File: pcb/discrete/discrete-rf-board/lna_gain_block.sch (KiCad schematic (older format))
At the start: 21 parts, among them Q801 Q_NPN_BCEE

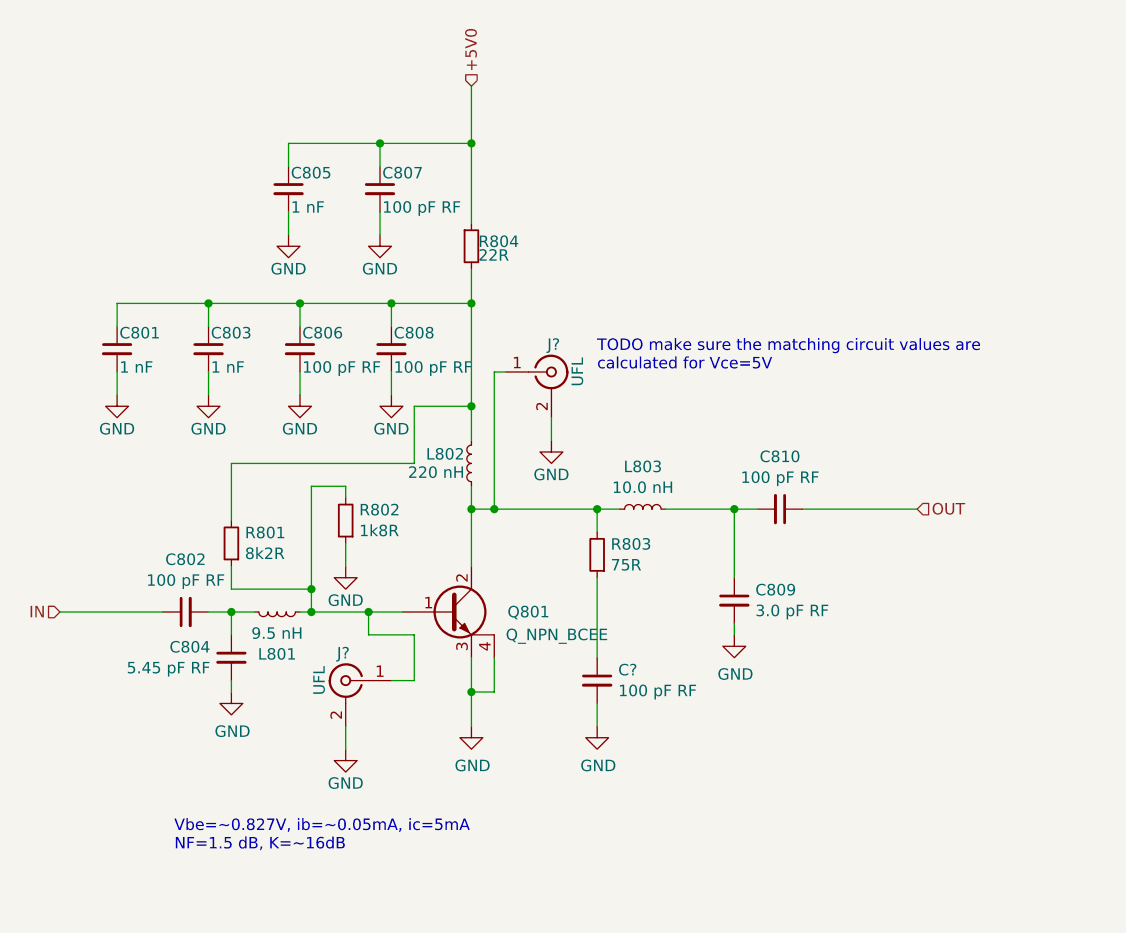
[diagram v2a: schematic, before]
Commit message: Start work in footprinting everything
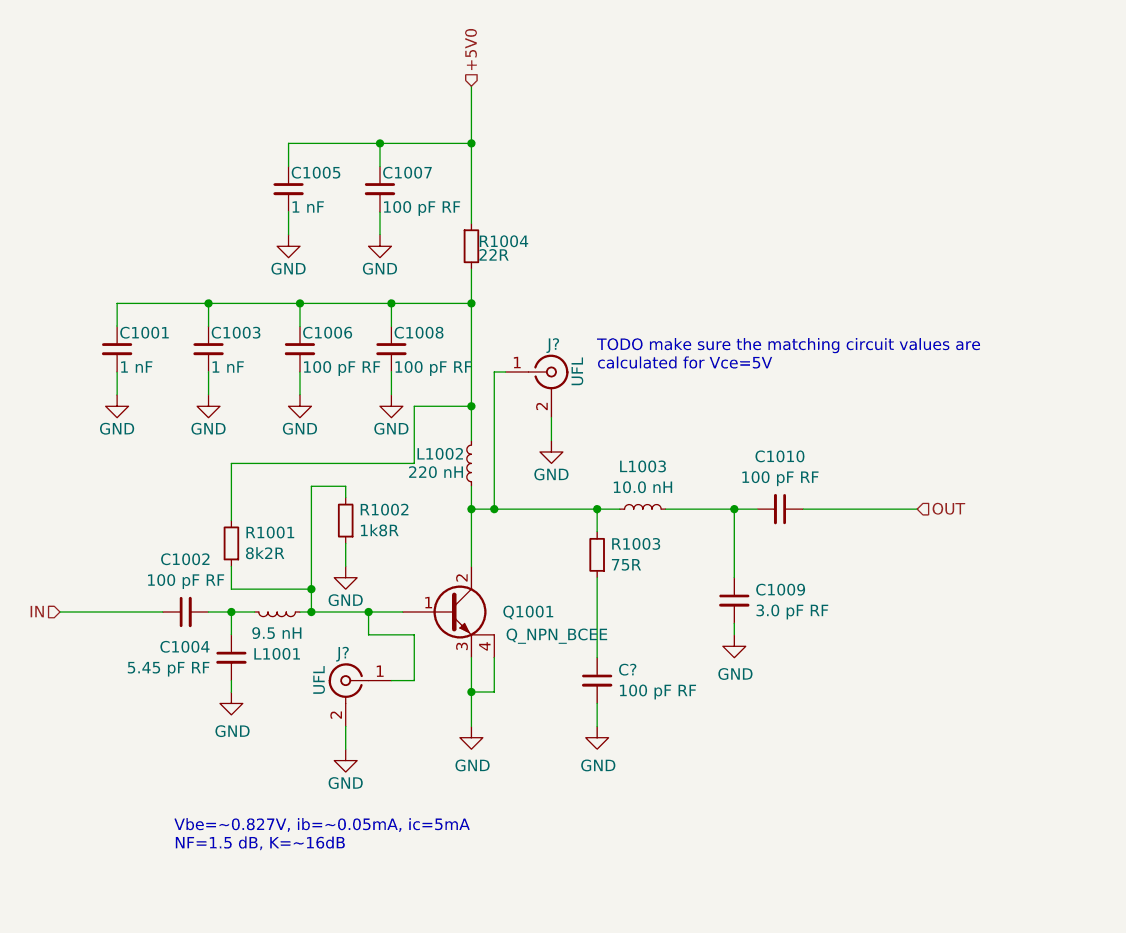
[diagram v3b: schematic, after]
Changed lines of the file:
@@
 AR Path="/5CA6B0AA/5CE74EBE/5D4104E7/5D3CF638" Ref="R903"  Part="1"
 AR Path="/5CA6B0AA/5CE74EBE/5D4124AC/5D3CF638" Ref="R1003"  Part="1"
-F 0 "R803" H 6041 3404 50  0000 R CNN
+F 0 "R1003" H 6041 3404 50  0000 R CNN
 F 1 "75R" H 6041 3495 50  0000 R CNN
 F 2 "" H 6100 3450 50  0001 C CNN
@@
 AR Path="/5CA6B0AA/5CE74EBE/5D4104E7/5D3CF640" Ref="C910"  Part="1"
 AR Path="/5CA6B0AA/5CE74EBE/5D4124AC/5D3CF640" Ref="C1010"  Part="1"
-F 0 "C810" V 7129 3250 50  0000 C CNN
+F 0 "C1010" V 7129 3250 50  0000 C CNN
 F 1 "100 pF RF" V 7038 3250 50  0000 C CNN
 F 2 "" H 6900 3250 50  0001 C CNN
@@
 AR Path="/5CA6B0AA/5CE74EBE/5D4104E7/5D3CF649" Ref="#PWR0903"  Part="1"
 AR Path="/5CA6B0AA/5CE74EBE/5D4124AC/5D3CF649" Ref="#PWR01003"  Part="1"
-F 0 "#PWR0803" H 4500 3800 50  0001 C CNN
+F 0 "#PWR01003" H 4500 3800 50  0001 C CNN
 F 1 "GND" H 4505 3877 50  0000 C CNN
 F 2 "" H 4500 4050 50  0001 C CNN
@@
 AR Path="/5CA6B0AA/5CE74EBE/5D4104E7/5D3CF650" Ref="#PWR0910"  Part="1"
 AR Path="/5CA6B0AA/5CE74EBE/5D4124AC/5D3CF650" Ref="#PWR01010"  Part="1"
-F 0 "#PWR0810" H 6700 3550 50  0001 C CNN
+F 0 "#PWR01010" H 6700 3550 50  0001 C CNN
 F 1 "GND" H 6705 3627 50  0000 C CNN
 F 2 "" H 6700 3800 50  0001 C CNN
@@
 AR Path="/5CA6B0AA/5CE74EBE/5D4104E7/5D3CF659" Ref="R901"  Part="1"
 AR Path="/5CA6B0AA/5CE74EBE/5D4124AC/5D3CF659" Ref="R1001"  Part="1"
-F 0 "R801" H 4441 3354 50  0000 R CNN
+F 0 "R1001" H 4441 3354 50  0000 R CNN
 F 1 "8k2R" H 4441 3445 50  0000 R CNN
 F 2 "" H 4500 3400 50  0001 C CNN
@@
 AR Path="/5CA6B0AA/5CE74EBE/5D4104E7/5D3CF668" Ref="C909"  Part="1"
 AR Path="/5CA6B0AA/5CE74EBE/5D4124AC/5D3CF668" Ref="C1009"  Part="1"
-F 0 "C809" H 6792 3696 50  0000 L CNN
+F 0 "C1009" H 6792 3696 50  0000 L CNN
 F 1 "3.0 pF RF" H 6792 3605 50  0000 L CNN
 F 2 "" H 6700 3650 50  0001 C CNN
@@
 AR Path="/5CA6B0AA/5CE74EBE/5D4104E7/5D3CF670" Ref="L903"  Part="1"
 AR Path="/5CA6B0AA/5CE74EBE/5D4124AC/5D3CF670" Ref="L1003"  Part="1"
-F 0 "L803" V 6485 3250 50  0000 C CNN
+F 0 "L1003" V 6485 3250 50  0000 C CNN
 F 1 "10.0 nH" V 6394 3250 50  0000 C CNN
 F 2 "" H 6300 3250 50  0001 C CNN
@@
 AR Path="/5CA6B0AA/5CE74EBE/5D4104E7/5D3CF693" Ref="C902"  Part="1"
 AR Path="/5CA6B0AA/5CE74EBE/5D4124AC/5D3CF693" Ref="C1002"  Part="1"
-F 0 "C802" V 4529 3700 50  0000 C CNN
+F 0 "C1002" V 4529 3700 50  0000 C CNN
 F 1 "100 pF RF" V 4438 3700 50  0000 C CNN
 F 2 "" H 4300 3700 50  0001 C CNN
@@
 AR Path="/5CA6B0AA/5CE74EBE/5D4104E7/5D3CF699" Ref="L901"  Part="1"
 AR Path="/5CA6B0AA/5CE74EBE/5D4124AC/5D3CF699" Ref="L1001"  Part="1"
-F 0 "L801" V 4885 3700 50  0000 C CNN
+F 0 "L1001" V 4885 3700 50  0000 C CNN
 F 1 "9.5 nH" V 4794 3700 50  0000 C CNN
 F 2 "" H 4700 3700 50  0001 C CNN
@@
 AR Path="/5CA6B0AA/5CE74EBE/5D4104E7/5D3CF69F" Ref="C904"  Part="1"
 AR Path="/5CA6B0AA/5CE74EBE/5D4124AC/5D3CF69F" Ref="C1004"  Part="1"
-F 0 "C804" H 4592 3946 50  0000 L CNN
+F 0 "C1004" H 4592 3946 50  0000 L CNN
 F 1 "5.45 pF RF" H 4592 3855 50  0000 L CNN
 F 2 "" H 4500 3900 50  0001 C CNN
@@
 AR Path="/5CA6B0AA/5CE74EBE/5D4104E7/5D3CF6A6" Ref="#PWR0909"  Part="1"
 AR Path="/5CA6B0AA/5CE74EBE/5D4124AC/5D3CF6A6" Ref="#PWR01009"  Part="1"
-F 0 "#PWR0809" H 5550 3950 50  0001 C CNN
+F 0 "#PWR01009" H 5550 3950 50  0001 C CNN
 F 1 "GND" H 5555 4027 50  0000 C CNN
 F 2 "" H 5550 4200 50  0001 C CNN
@@
 AR Path="/5CA6B0AA/5CE74EBE/5D4104E7/5D3E5B01" Ref="C903"  Part="1"
 AR Path="/5CA6B0AA/5CE74EBE/5D4124AC/5D3E5B01" Ref="C1003"  Part="1"
-F 0 "C803" H 4410 2620 50  0000 L CNN
+F 0 "C1003" H 4410 2620 50  0000 L CNN
 F 1 "1 nF" H 4410 2470 50  0000 L CNN
 F 2 "" H 4400 2550 50  0001 C CNN
@@
 AR Path="/5CA6B0AA/5CE74EBE/5D4104E7/5D3E5B07" Ref="C906"  Part="1"
 AR Path="/5CA6B0AA/5CE74EBE/5D4124AC/5D3E5B07" Ref="C1006"  Part="1"
-F 0 "C806" H 4810 2620 50  0000 L CNN
+F 0 "C1006" H 4810 2620 50  0000 L CNN
 F 1 "100 pF RF" H 4810 2470 50  0000 L CNN
 F 2 "" H 4800 2550 50  0001 C CNN
@@
 AR Path="/5CA6B0AA/5CE74EBE/5D4104E7/5D3E5B0D" Ref="C908"  Part="1"
 AR Path="/5CA6B0AA/5CE74EBE/5D4124AC/5D3E5B0D" Ref="C1008"  Part="1"
-F 0 "C808" H 5210 2620 50  0000 L CNN
+F 0 "C1008" H 5210 2620 50  0000 L CNN
 F 1 "100 pF RF" H 5210 2470 50  0000 L CNN
 F 2 "" H 5200 2550 50  0001 C CNN
@@
 AR Path="/5CA6B0AA/5CE74EBE/5D4104E7/5D3E5B13" Ref="#PWR0902"  Part="1"
 AR Path="/5CA6B0AA/5CE74EBE/5D4124AC/5D3E5B13" Ref="#PWR01002"  Part="1"
-F 0 "#PWR0802" H 4400 2500 50  0001 C CNN
+F 0 "#PWR01002" H 4400 2500 50  0001 C CNN
 F 1 "GND" H 4400 2600 50  0000 C CNN
 F 2 "" H 4400 2750 50  0001 C CNN
@@
 AR Path="/5CA6B0AA/5CE74EBE/5D4104E7/5D3E5B19" Ref="#PWR0905"  Part="1"
 AR Path="/5CA6B0AA/5CE74EBE/5D4124AC/5D3E5B19" Ref="#PWR01005"  Part="1"
-F 0 "#PWR0805" H 4800 2500 50  0001 C CNN
+F 0 "#PWR01005" H 4800 2500 50  0001 C CNN
 F 1 "GND" H 4800 2600 50  0000 C CNN
 F 2 "" H 4800 2750 50  0001 C CNN
@@
 AR Path="/5CA6B0AA/5CE74EBE/5D4104E7/5D3E5B1F" Ref="#PWR0908"  Part="1"
 AR Path="/5CA6B0AA/5CE74EBE/5D4124AC/5D3E5B1F" Ref="#PWR01008"  Part="1"
-F 0 "#PWR0808" H 5200 2500 50  0001 C CNN
+F 0 "#PWR01008" H 5200 2500 50  0001 C CNN
 F 1 "GND" H 5200 2600 50  0000 C CNN
 F 2 "" H 5200 2750 50  0001 C CNN
@@
 AR Path="/5CA6B0AA/5CE74EBE/5D4104E7/5D3E5B25" Ref="C907"  Part="1"
 AR Path="/5CA6B0AA/5CE74EBE/5D4124AC/5D3E5B25" Ref="C1007"  Part="1"
-F 0 "C807" H 5160 1920 50  0000 L CNN
+F 0 "C1007" H 5160 1920 50  0000 L CNN
 F 1 "100 pF RF" H 5160 1770 50  0000 L CNN
 F 2 "" H 5150 1850 50  0001 C CNN
@@
 AR Path="/5CA6B0AA/5CE74EBE/5D4104E7/5D3E5B2B" Ref="#PWR0907"  Part="1"
 AR Path="/5CA6B0AA/5CE74EBE/5D4124AC/5D3E5B2B" Ref="#PWR01007"  Part="1"
-F 0 "#PWR0807" H 5150 1800 50  0001 C CNN
+F 0 "#PWR01007" H 5150 1800 50  0001 C CNN
 F 1 "GND" H 5150 1900 50  0000 C CNN
 F 2 "" H 5150 2050 50  0001 C CNN
@@
 AR Path="/5CA6B0AA/5CE74EBE/5D4104E7/5D3E5B31" Ref="C905"  Part="1"
 AR Path="/5CA6B0AA/5CE74EBE/5D4124AC/5D3E5B31" Ref="C1005"  Part="1"
-F 0 "C805" H 4760 1920 50  0000 L CNN
+F 0 "C1005" H 4760 1920 50  0000 L CNN
 F 1 "1 nF" H 4760 1770 50  0000 L CNN
 F 2 "" H 4750 1850 50  0001 C CNN
@@
 AR Path="/5CA6B0AA/5CE74EBE/5D4104E7/5D3E5B37" Ref="#PWR0904"  Part="1"
 AR Path="/5CA6B0AA/5CE74EBE/5D4124AC/5D3E5B37" Ref="#PWR01004"  Part="1"
-F 0 "#PWR0804" H 4750 1800 50  0001 C CNN
+F 0 "#PWR01004" H 4750 1800 50  0001 C CNN
 F 1 "GND" H 4750 1900 50  0000 C CNN
 F 2 "" H 4750 2050 50  0001 C CNN
@@
 AR Path="/5CA6B0AA/5CE74EBE/5D4104E7/5D3F1C48" Ref="R904"  Part="1"
 AR Path="/5CA6B0AA/5CE74EBE/5D4124AC/5D3F1C48" Ref="R1004"  Part="1"
-F 0 "R804" H 5580 2120 50  0000 L CNN
+F 0 "R1004" H 5580 2120 50  0000 L CNN
 F 1 "22R" H 5580 2060 50  0000 L CNN
 F 2 "" H 5550 2100 50  0001 C CNN
@@
 AR Path="/5CA6B0AA/5CE74EBE/5D4104E7/5D3FEB6E" Ref="C901"  Part="1"
 AR Path="/5CA6B0AA/5CE74EBE/5D4124AC/5D3FEB6E" Ref="C1001"  Part="1"
-F 0 "C801" H 4010 2620 50  0000 L CNN
+F 0 "C1001" H 4010 2620 50  0000 L CNN
 F 1 "1 nF" H 4010 2470 50  0000 L CNN
 F 2 "" H 4000 2550 50  0001 C CNN
@@
 AR Path="/5CA6B0AA/5CE74EBE/5D4104E7/5D3FEB74" Ref="#PWR0901"  Part="1"
 AR Path="/5CA6B0AA/5CE74EBE/5D4124AC/5D3FEB74" Ref="#PWR01001"  Part="1"
-F 0 "#PWR0801" H 4000 2500 50  0001 C CNN
+F 0 "#PWR01001" H 4000 2500 50  0001 C CNN
 F 1 "GND" H 4000 2600 50  0000 C CNN
 F 2 "" H 4000 2750 50  0001 C CNN
@@
 AR Path="/5CA6B0AA/5CE74EBE/5D4104E7/5D40D244" Ref="L902"  Part="1"
 AR Path="/5CA6B0AA/5CE74EBE/5D4124AC/5D40D244" Ref="L1002"  Part="1"
-F 0 "L802" H 5580 3090 50  0000 L CNN
+F 0 "L1002" H 5580 3090 50  0000 L CNN
 F 1 "220 nH" H 5580 3010 50  0000 L CNN
 F 2 "" H 5550 3050 50  0001 C CNN
@@
 AR Path="/5CA6B0AA/5CE74EBE/5D4104E7/5D435867" Ref="R902"  Part="1"
 AR Path="/5CA6B0AA/5CE74EBE/5D4124AC/5D435867" Ref="R1002"  Part="1"
-F 0 "R802" H 4941 3254 50  0000 R CNN
+F 0 "R1002" H 4941 3254 50  0000 R CNN
 F 1 "1k8R" H 4941 3345 50  0000 R CNN
 F 2 "" H 5000 3300 50  0001 C CNN
@@
 AR Path="/5CA6B0AA/5CE74EBE/5D3C8D48/5D43681D" Ref="#PWR0806"  Part="1"
 AR Path="/5CA6B0AA/5CE74EBE/5D4104E7/5D43681D" Ref="#PWR0906"  Part="1"
-F 0 "#PWR0806" H 5000 3250 50  0001 C CNN
+F 0 "#PWR01006" H 5000 3250 50  0001 C CNN
 F 1 "GND" H 5000 3350 50  0000 C CNN
 F 2 "" H 5000 3500 50  0001 C CNN
@@
 AR Path="/5CA6B0AA/5CE74EBE/5D4104E7/5D191C23" Ref="Q901"  Part="1"
 AR Path="/5CA6B0AA/5CE74EBE/5D4124AC/5D191C23" Ref="Q1001"  Part="1"
-F 0 "Q801" H 5800 3700 50  0000 C CNN
+F 0 "Q1001" H 5800 3700 50  0000 C CNN
 F 1 "Q_NPN_BCEE" H 5700 3600 50  0000 L CNN
 F 2 "" H 5500 3700 50  0001 C CNN

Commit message: Fix some parts
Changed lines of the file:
@@
 $Descr A4 11693 8268
 encoding utf-8
-Sheet 16 19
+Sheet 14 19
 Title ""
 Date ""
@@
 AR Path="/5CA6B0AA/5CE74EBE/5D4104E7/5D3CF638" Ref="R903"  Part="1"
 AR Path="/5CA6B0AA/5CE74EBE/5D4124AC/5D3CF638" Ref="R1003"  Part="1"
-F 0 "R1003" H 6041 3404 50  0000 R CNN
+F 0 "R803" H 6041 3404 50  0000 R CNN
 F 1 "75R" H 6041 3495 50  0000 R CNN
 F 2 "" H 6100 3450 50  0001 C CNN
@@
 AR Path="/5CA6B0AA/5CE74EBE/5D4104E7/5D3CF640" Ref="C910"  Part="1"
 AR Path="/5CA6B0AA/5CE74EBE/5D4124AC/5D3CF640" Ref="C1010"  Part="1"
-F 0 "C1010" V 7129 3250 50  0000 C CNN
+F 0 "C810" V 7129 3250 50  0000 C CNN
 F 1 "100 pF RF" V 7038 3250 50  0000 C CNN
 F 2 "" H 6900 3250 50  0001 C CNN
@@
 AR Path="/5CA6B0AA/5CE74EBE/5D4104E7/5D3CF649" Ref="#PWR0903"  Part="1"
 AR Path="/5CA6B0AA/5CE74EBE/5D4124AC/5D3CF649" Ref="#PWR01003"  Part="1"
-F 0 "#PWR01003" H 4500 3800 50  0001 C CNN
+F 0 "#PWR0803" H 4500 3800 50  0001 C CNN
 F 1 "GND" H 4505 3877 50  0000 C CNN
 F 2 "" H 4500 4050 50  0001 C CNN
@@
 AR Path="/5CA6B0AA/5CE74EBE/5D4104E7/5D3CF650" Ref="#PWR0910"  Part="1"
 AR Path="/5CA6B0AA/5CE74EBE/5D4124AC/5D3CF650" Ref="#PWR01010"  Part="1"
-F 0 "#PWR01010" H 6700 3550 50  0001 C CNN
+F 0 "#PWR0810" H 6700 3550 50  0001 C CNN
 F 1 "GND" H 6705 3627 50  0000 C CNN
 F 2 "" H 6700 3800 50  0001 C CNN
@@
 AR Path="/5CA6B0AA/5CE74EBE/5D4104E7/5D3CF659" Ref="R901"  Part="1"
 AR Path="/5CA6B0AA/5CE74EBE/5D4124AC/5D3CF659" Ref="R1001"  Part="1"
-F 0 "R1001" H 4441 3354 50  0000 R CNN
+F 0 "R801" H 4441 3354 50  0000 R CNN
 F 1 "8k2R" H 4441 3445 50  0000 R CNN
 F 2 "" H 4500 3400 50  0001 C CNN
@@
 AR Path="/5CA6B0AA/5CE74EBE/5D4104E7/5D3CF668" Ref="C909"  Part="1"
 AR Path="/5CA6B0AA/5CE74EBE/5D4124AC/5D3CF668" Ref="C1009"  Part="1"
-F 0 "C1009" H 6792 3696 50  0000 L CNN
+F 0 "C809" H 6792 3696 50  0000 L CNN
 F 1 "3.0 pF RF" H 6792 3605 50  0000 L CNN
 F 2 "" H 6700 3650 50  0001 C CNN
@@
 AR Path="/5CA6B0AA/5CE74EBE/5D4104E7/5D3CF670" Ref="L903"  Part="1"
 AR Path="/5CA6B0AA/5CE74EBE/5D4124AC/5D3CF670" Ref="L1003"  Part="1"
-F 0 "L1003" V 6485 3250 50  0000 C CNN
+F 0 "L803" V 6485 3250 50  0000 C CNN
 F 1 "10.0 nH" V 6394 3250 50  0000 C CNN
 F 2 "" H 6300 3250 50  0001 C CNN
@@
 AR Path="/5CA6B0AA/5CE74EBE/5D4104E7/5D3CF693" Ref="C902"  Part="1"
 AR Path="/5CA6B0AA/5CE74EBE/5D4124AC/5D3CF693" Ref="C1002"  Part="1"
-F 0 "C1002" V 4529 3700 50  0000 C CNN
+F 0 "C802" V 4529 3700 50  0000 C CNN
 F 1 "100 pF RF" V 4438 3700 50  0000 C CNN
 F 2 "" H 4300 3700 50  0001 C CNN
@@
 AR Path="/5CA6B0AA/5CE74EBE/5D4104E7/5D3CF699" Ref="L901"  Part="1"
 AR Path="/5CA6B0AA/5CE74EBE/5D4124AC/5D3CF699" Ref="L1001"  Part="1"
-F 0 "L1001" V 4885 3700 50  0000 C CNN
+F 0 "L801" V 4885 3700 50  0000 C CNN
 F 1 "9.5 nH" V 4794 3700 50  0000 C CNN
 F 2 "" H 4700 3700 50  0001 C CNN
@@
 AR Path="/5CA6B0AA/5CE74EBE/5D4104E7/5D3CF69F" Ref="C904"  Part="1"
 AR Path="/5CA6B0AA/5CE74EBE/5D4124AC/5D3CF69F" Ref="C1004"  Part="1"
-F 0 "C1004" H 4592 3946 50  0000 L CNN
+F 0 "C804" H 4592 3946 50  0000 L CNN
 F 1 "5.45 pF RF" H 4592 3855 50  0000 L CNN
 F 2 "" H 4500 3900 50  0001 C CNN
@@
 AR Path="/5CA6B0AA/5CE74EBE/5D4104E7/5D3CF6A6" Ref="#PWR0909"  Part="1"
 AR Path="/5CA6B0AA/5CE74EBE/5D4124AC/5D3CF6A6" Ref="#PWR01009"  Part="1"
-F 0 "#PWR01009" H 5550 3950 50  0001 C CNN
+F 0 "#PWR0809" H 5550 3950 50  0001 C CNN
 F 1 "GND" H 5555 4027 50  0000 C CNN
 F 2 "" H 5550 4200 50  0001 C CNN
@@
 AR Path="/5CA6B0AA/5CE74EBE/5D4104E7/5D3E5B01" Ref="C903"  Part="1"
 AR Path="/5CA6B0AA/5CE74EBE/5D4124AC/5D3E5B01" Ref="C1003"  Part="1"
-F 0 "C1003" H 4410 2620 50  0000 L CNN
+F 0 "C803" H 4410 2620 50  0000 L CNN
 F 1 "1 nF" H 4410 2470 50  0000 L CNN
 F 2 "" H 4400 2550 50  0001 C CNN
@@
 AR Path="/5CA6B0AA/5CE74EBE/5D4104E7/5D3E5B07" Ref="C906"  Part="1"
 AR Path="/5CA6B0AA/5CE74EBE/5D4124AC/5D3E5B07" Ref="C1006"  Part="1"
-F 0 "C1006" H 4810 2620 50  0000 L CNN
+F 0 "C806" H 4810 2620 50  0000 L CNN
 F 1 "100 pF RF" H 4810 2470 50  0000 L CNN
 F 2 "" H 4800 2550 50  0001 C CNN
@@
 AR Path="/5CA6B0AA/5CE74EBE/5D4104E7/5D3E5B0D" Ref="C908"  Part="1"
 AR Path="/5CA6B0AA/5CE74EBE/5D4124AC/5D3E5B0D" Ref="C1008"  Part="1"
-F 0 "C1008" H 5210 2620 50  0000 L CNN
+F 0 "C808" H 5210 2620 50  0000 L CNN
 F 1 "100 pF RF" H 5210 2470 50  0000 L CNN
 F 2 "" H 5200 2550 50  0001 C CNN
@@
 AR Path="/5CA6B0AA/5CE74EBE/5D4104E7/5D3E5B13" Ref="#PWR0902"  Part="1"
 AR Path="/5CA6B0AA/5CE74EBE/5D4124AC/5D3E5B13" Ref="#PWR01002"  Part="1"
-F 0 "#PWR01002" H 4400 2500 50  0001 C CNN
+F 0 "#PWR0802" H 4400 2500 50  0001 C CNN
 F 1 "GND" H 4400 2600 50  0000 C CNN
 F 2 "" H 4400 2750 50  0001 C CNN
@@
 AR Path="/5CA6B0AA/5CE74EBE/5D4104E7/5D3E5B19" Ref="#PWR0905"  Part="1"
 AR Path="/5CA6B0AA/5CE74EBE/5D4124AC/5D3E5B19" Ref="#PWR01005"  Part="1"
-F 0 "#PWR01005" H 4800 2500 50  0001 C CNN
+F 0 "#PWR0805" H 4800 2500 50  0001 C CNN
 F 1 "GND" H 4800 2600 50  0000 C CNN
 F 2 "" H 4800 2750 50  0001 C CNN
@@
 AR Path="/5CA6B0AA/5CE74EBE/5D4104E7/5D3E5B1F" Ref="#PWR0908"  Part="1"
 AR Path="/5CA6B0AA/5CE74EBE/5D4124AC/5D3E5B1F" Ref="#PWR01008"  Part="1"
-F 0 "#PWR01008" H 5200 2500 50  0001 C CNN
+F 0 "#PWR0808" H 5200 2500 50  0001 C CNN
 F 1 "GND" H 5200 2600 50  0000 C CNN
 F 2 "" H 5200 2750 50  0001 C CNN
@@
 AR Path="/5CA6B0AA/5CE74EBE/5D4104E7/5D3E5B25" Ref="C907"  Part="1"
 AR Path="/5CA6B0AA/5CE74EBE/5D4124AC/5D3E5B25" Ref="C1007"  Part="1"
-F 0 "C1007" H 5160 1920 50  0000 L CNN
+F 0 "C807" H 5160 1920 50  0000 L CNN
 F 1 "100 pF RF" H 5160 1770 50  0000 L CNN
 F 2 "" H 5150 1850 50  0001 C CNN
@@
 AR Path="/5CA6B0AA/5CE74EBE/5D4104E7/5D3E5B2B" Ref="#PWR0907"  Part="1"
 AR Path="/5CA6B0AA/5CE74EBE/5D4124AC/5D3E5B2B" Ref="#PWR01007"  Part="1"
-F 0 "#PWR01007" H 5150 1800 50  0001 C CNN
+F 0 "#PWR0807" H 5150 1800 50  0001 C CNN
 F 1 "GND" H 5150 1900 50  0000 C CNN
 F 2 "" H 5150 2050 50  0001 C CNN
@@
 AR Path="/5CA6B0AA/5CE74EBE/5D4104E7/5D3E5B31" Ref="C905"  Part="1"
 AR Path="/5CA6B0AA/5CE74EBE/5D4124AC/5D3E5B31" Ref="C1005"  Part="1"
-F 0 "C1005" H 4760 1920 50  0000 L CNN
+F 0 "C805" H 4760 1920 50  0000 L CNN
 F 1 "1 nF" H 4760 1770 50  0000 L CNN
 F 2 "" H 4750 1850 50  0001 C CNN
@@
 AR Path="/5CA6B0AA/5CE74EBE/5D4104E7/5D3E5B37" Ref="#PWR0904"  Part="1"
 AR Path="/5CA6B0AA/5CE74EBE/5D4124AC/5D3E5B37" Ref="#PWR01004"  Part="1"
-F 0 "#PWR01004" H 4750 1800 50  0001 C CNN
+F 0 "#PWR0804" H 4750 1800 50  0001 C CNN
 F 1 "GND" H 4750 1900 50  0000 C CNN
 F 2 "" H 4750 2050 50  0001 C CNN
@@
 AR Path="/5CA6B0AA/5CE74EBE/5D4104E7/5D3F1C48" Ref="R904"  Part="1"
 AR Path="/5CA6B0AA/5CE74EBE/5D4124AC/5D3F1C48" Ref="R1004"  Part="1"
-F 0 "R1004" H 5580 2120 50  0000 L CNN
+F 0 "R804" H 5580 2120 50  0000 L CNN
 F 1 "22R" H 5580 2060 50  0000 L CNN
 F 2 "" H 5550 2100 50  0001 C CNN
@@
 AR Path="/5CA6B0AA/5CE74EBE/5D4104E7/5D3FEB6E" Ref="C901"  Part="1"
 AR Path="/5CA6B0AA/5CE74EBE/5D4124AC/5D3FEB6E" Ref="C1001"  Part="1"
-F 0 "C1001" H 4010 2620 50  0000 L CNN
+F 0 "C801" H 4010 2620 50  0000 L CNN
 F 1 "1 nF" H 4010 2470 50  0000 L CNN
 F 2 "" H 4000 2550 50  0001 C CNN
@@
 AR Path="/5CA6B0AA/5CE74EBE/5D4104E7/5D3FEB74" Ref="#PWR0901"  Part="1"
 AR Path="/5CA6B0AA/5CE74EBE/5D4124AC/5D3FEB74" Ref="#PWR01001"  Part="1"
-F 0 "#PWR01001" H 4000 2500 50  0001 C CNN
+F 0 "#PWR0801" H 4000 2500 50  0001 C CNN
 F 1 "GND" H 4000 2600 50  0000 C CNN
 F 2 "" H 4000 2750 50  0001 C CNN
@@
 AR Path="/5CA6B0AA/5CE74EBE/5D4104E7/5D40D244" Ref="L902"  Part="1"
 AR Path="/5CA6B0AA/5CE74EBE/5D4124AC/5D40D244" Ref="L1002"  Part="1"
-F 0 "L1002" H 5580 3090 50  0000 L CNN
+F 0 "L802" H 5580 3090 50  0000 L CNN
 F 1 "220 nH" H 5580 3010 50  0000 L CNN
 F 2 "" H 5550 3050 50  0001 C CNN
@@
 AR Path="/5CA6B0AA/5CE74EBE/5D4104E7/5D435867" Ref="R902"  Part="1"
 AR Path="/5CA6B0AA/5CE74EBE/5D4124AC/5D435867" Ref="R1002"  Part="1"
-F 0 "R1002" H 4941 3254 50  0000 R CNN
+F 0 "R802" H 4941 3254 50  0000 R CNN
 F 1 "1k8R" H 4941 3345 50  0000 R CNN
 F 2 "" H 5000 3300 50  0001 C CNN
@@
 AR Path="/5CA6B0AA/5CE74EBE/5D3C8D48/5D43681D" Ref="#PWR0806"  Part="1"
 AR Path="/5CA6B0AA/5CE74EBE/5D4104E7/5D43681D" Ref="#PWR0906"  Part="1"
-F 0 "#PWR01006" H 5000 3250 50  0001 C CNN
+F 0 "#PWR0806" H 5000 3250 50  0001 C CNN
 F 1 "GND" H 5000 3350 50  0000 C CNN
 F 2 "" H 5000 3500 50  0001 C CNN
@@
 AR Path="/5CA6B0AA/5CE74EBE/5D4104E7/5D191C23" Ref="Q901"  Part="1"
 AR Path="/5CA6B0AA/5CE74EBE/5D4124AC/5D191C23" Ref="Q1001"  Part="1"
-F 0 "Q1001" H 5800 3700 50  0000 C CNN
+F 0 "Q801" H 5800 3700 50  0000 C CNN
 F 1 "Q_NPN_BCEE" H 5700 3600 50  0000 L CNN
 F 2 "" H 5500 3700 50  0001 C CNN
